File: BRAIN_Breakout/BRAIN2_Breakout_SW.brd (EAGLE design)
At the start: 96.9 x 68.4 mm, 101 parts

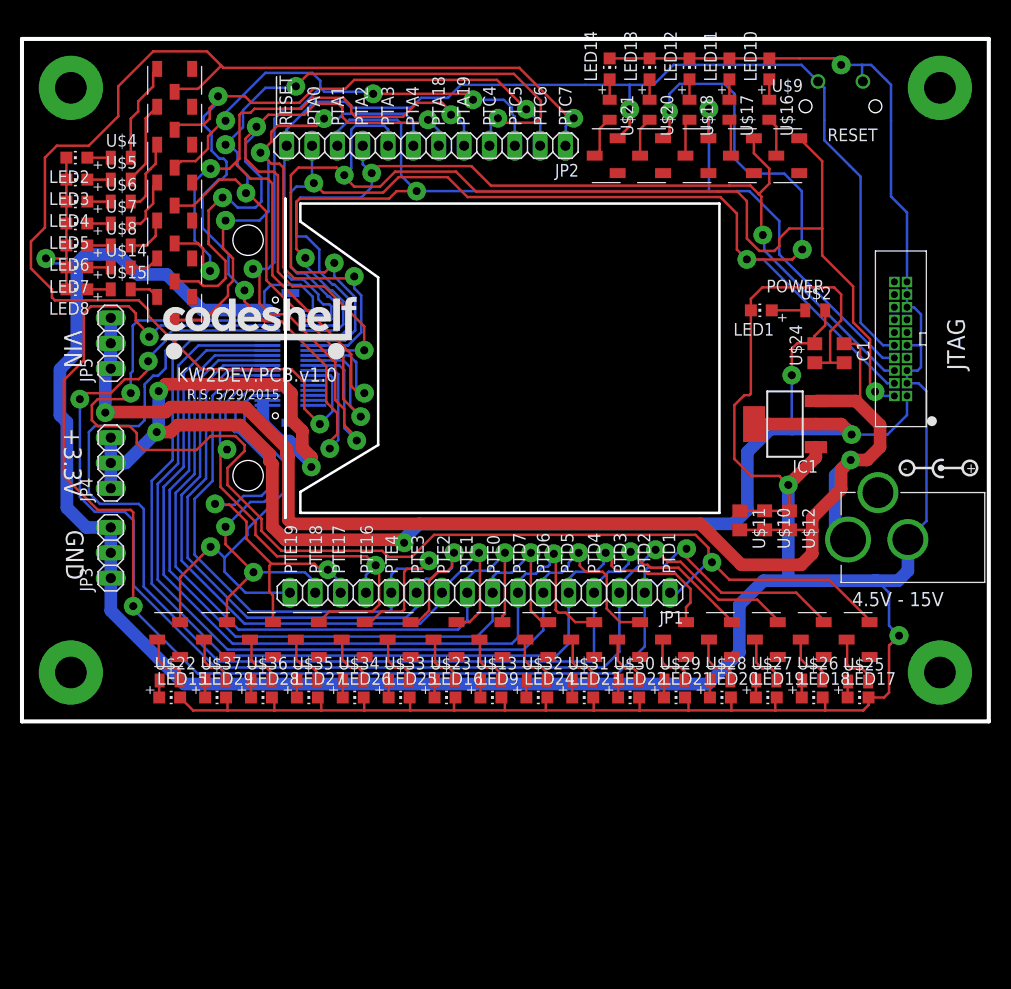
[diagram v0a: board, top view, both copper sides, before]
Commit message: Added board for new KW2
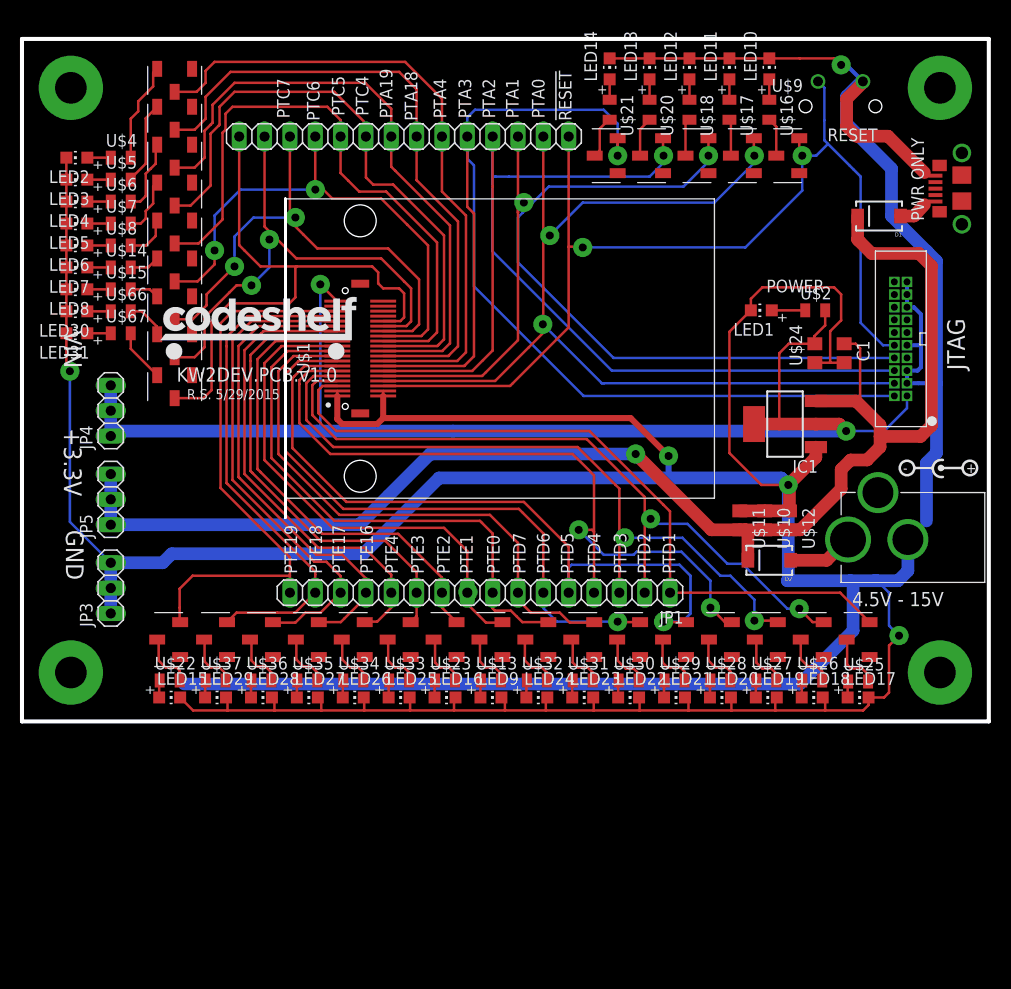
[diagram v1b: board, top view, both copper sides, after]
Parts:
- added D1, D2: (no value), SparkFun:SMA-DIODE
- added LED30, LED31: (no value), adafruit:CHIP-LED0805
- added U$66, U$67: (no value), GW-devices:RF-C0805
- added U$68, U$69: CJS, KW2:CJS
- added X1: USB, SparkFun:USB3076-30-A
- JP2: device pinhead:1X12 -> pinhead:1X14
- U$1: value DF12_F -> KW2_CPU_NEW; device KW2:DF12_F -> KW2:BRAIN_NEW
- U$2: value (none) -> 1k
- U$21: value (none) -> 2k
- moved JP5 15.6 mm to (42.0, 35.4)
- moved U$1 7.06 mm to (67.0, 50.5), flipped to the top, turned to 90 degrees
- moved JP4 5.24 mm to (42.0, 44.2)
- moved JP3 3.54 mm to (42.0, 26.5)
- moved JP2 2.40 mm to (71.4, 71.7), turned to 0 degrees
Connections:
- removed net N$51: JP2.9, U$1.P$12, U$19.P$6, U$55.P$3
- new net N$71: D2.A, U$3.P$1
- new net N$72: D1.A, X1.VCC
- new net N$73: JP2.1, U$1.P$32, U$69.P$1
- new net N$75: LED30.A, U$66.1
- new net N$76: LED31.A, U$67.1
- new net N$77: U$67.2, U$69.P$3
- new net N$78: U$66.2, U$68.P$3
- new net N$80: JP2.2, U$1.P$30, U$68.P$1
- new net N$86: JP2.11, U$1.P$12, U$19.P$6, U$57.P$3
- net GND: now also LED30.C, LED31.C, X1.GND
- net N$21: now also JP2.3, U$65.P$1; no longer JP2.1, U$59.P$1
- net N$22: now also JP2.4, U$64.P$1; no longer JP2.2, U$60.P$1
- net N$23: now also JP2.5, U$63.P$1; no longer JP2.3, U$61.P$1
- net N$24: now also JP2.6; no longer JP2.4
- net N$25: now also JP2.7, U$61.P$1; no longer JP2.5, U$63.P$1
- net N$26: now also JP2.8, U$60.P$1; no longer JP2.6, U$64.P$1
- net N$27: now also JP2.9, U$59.P$1; no longer JP2.7, U$65.P$1
- net N$48: now also JP2.10, U$58.P$3; no longer JP2.8, U$54.P$3
- net N$54: now also JP2.12; no longer JP2.10
- net N$57: now also JP2.13, U$55.P$3; no longer JP2.11, U$57.P$3
- net N$60: now also JP2.14, U$54.P$3; no longer JP2.12, U$58.P$3
- net V+: now also D1.C, D2.C; no longer U$3.P$1
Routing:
- net N$86: track 0.00 -> 110.5 mm, vias 0 -> 1
- net N$51: track 102.9 -> 0.00 mm, vias 2 -> 0
- net GND: track 436.8 -> 533.9 mm, vias 4 -> 5
- net N$21: track 127.5 -> 51.5 mm
- net PTD2: track 141.5 -> 74.2 mm, vias 3 -> 2
- net N$73: track 0.00 -> 58.2 mm
- net PTD1: track 128.0 -> 73.1 mm, vias 2 -> 0
- net PTD3: track 125.1 -> 72.4 mm, vias 3 -> 2
- net N$80: track 0.00 -> 50.9 mm, vias 0 -> 2
- net N$22: track 99.8 -> 53.2 mm, vias 4 -> 2
- net PTD4: track 119.7 -> 74.6 mm, vias 1 -> 2
- net N$23: track 100.8 -> 61.5 mm, vias 5 -> 0
- net +3V3: track 167.8 -> 129.7 mm, vias 6 -> 2
- net N$24: track 98.1 -> 61.7 mm, vias 5 -> 0
- net PTD6: track 96.0 -> 60.5 mm
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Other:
- outline, holes or cut-outs redrawn
- board text added: "PWR ONLY"

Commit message: sync repo
Get the DEVBDS work in sync
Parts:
- added IC2: FT2232HL, KW2:LQFP64
- moved LED1 7.03 mm to (109.0, 47.5), turned to 270 degrees
- moved U$2 6.00 mm to (109.0, 49.5)
- moved C1 1.50 mm to (115.5, 48.5)
- moved U$24 1.50 mm to (112.6, 48.5)
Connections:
- new net N$82: X1.D-
- new net N$83: X1.D+
- net GND: now also X1.P$4
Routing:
- net +3V3: track 129.7 -> 117.4 mm
- net GND: track 533.9 -> 525.9 mm
- net N$1: track 3.35 -> 2.02 mm
- net V+: track 145.3 -> 144.1 mm
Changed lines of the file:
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@@
 <setting verticaltext="up"/>
 </settings>
-<grid distance="1" unitdist="mm" unit="mm" style="lines" multiple="1" display="yes" altdistance="0.05" altunitdist="mm" altunit="mm"/>
+<grid distance="0.5" unitdist="mm" unit="mm" style="lines" multiple="1" display="yes" altdistance="0.05" altunitdist="mm" altunit="mm"/>
 <layers>
 <layer number="1" name="Top" color="4" fill="1" visible="yes" active="yes"/>
@@
 <attribute name="MFGP" value="NCP1117ST33T3G" x="109.57" y="42.9" size="1.778" layer="27" rot="R90" display="off"/>
 </element>
-<element name="U$24" library="GW-devices" package="C0805" value="" x="112.56" y="50" rot="R90">
-<attribute name="MFGN" value="Murata" x="112.56" y="50" size="1.778" layer="27" rot="R90" display="off"/>
-<attribute name="MFGP" value="GRM219R61E106KA12D" x="112.56" y="50" size="1.778" layer="27" rot="R90" display="off"/>
+<element name="U$24" library="GW-devices" package="C0805" value="" x="112.56" y="48.5" rot="R90">
+<attribute name="MFGN" value="Murata" x="112.56" y="48.5" size="1.778" layer="27" rot="R90" display="off"/>
+<attribute name="MFGP" value="GRM219R61E106KA12D" x="112.56" y="48.5" size="1.778" layer="27" rot="R90" display="off"/>
 </element>
 <element name="U$3" library="KW2" package="BARREL_CUI_PJ-002A" value="BARREL_CUI_PJ-002A" x="115.89" y="31.33" smashed="yes">
@@
 <attribute name="MFGP" value="PRPC003SAAN-RC" x="42" y="35.35" size="1.778" layer="27" rot="R90" display="off"/>
 </element>
-<element name="LED1" library="adafruit" package="CHIP-LED0805" value="" x="107.2" y="54.3" rot="R90">
-<attribute name="MFGN" value="Wurth Electronics Inc" x="107.2" y="54.3" size="1.778" layer="27" rot="R90" display="off"/>
-<attribute name="MFGP" value="150080BS75000" x="107.2" y="54.3" size="1.778" layer="27" rot="R90" display="off"/>
-</element>
-<element name="U$2" library="GW-devices" package="RF-C0805" value="1k" x="112.6" y="54.3">
-<attribute name="MFGN" value="Panasonic" x="112.6" y="54.3" size="1.778" layer="27" display="off"/>
-<attribute name="MFGP" value="ERJ-6ENF2000V" x="112.6" y="54.3" size="1.778" layer="27" display="off"/>
+<element name="LED1" library="adafruit" package="CHIP-LED0805" value="" x="109" y="47.5" rot="R270">
+<attribute name="MFGN" value="Wurth Electronics Inc" x="109" y="47.5" size="1.778" layer="27" rot="R270" display="off"/>
+<attribute name="MFGP" value="150080BS75000" x="109" y="47.5" size="1.778" layer="27" rot="R270" display="off"/>
+</element>
+<element name="U$2" library="GW-devices" package="RF-C0805" value="1k" x="109" y="49.5">
+<attribute name="MFGN" value="Panasonic" x="109" y="49.5" size="1.778" layer="27" display="off"/>
+<attribute name="MFGP" value="ERJ-6ENF2000V" x="109" y="49.5" size="1.778" layer="27" display="off"/>
 </element>
 <element name="LED2" library="adafruit" package="CHIP-LED0805" value="" x="38.6" y="69.6" rot="R90">
@@
 <attribute name="MFGP" value="ERJ-6ENF2001V" x="43" y="56.4" size="1.778" layer="27" display="off"/>
 </element>
-<element name="C1" library="GW-devices" package="C0805" value="" x="115.5" y="50" rot="R270">
-<attribute name="MFGN" value="Murata" x="115.5" y="50" size="1.778" layer="27" rot="R270" display="off"/>
-<attribute name="MFGP" value="GRM219R61E106KA12D" x="115.5" y="50" size="1.778" layer="27" rot="R270" display="off"/>
+<element name="C1" library="GW-devices" package="C0805" value="" x="115.5" y="48.5" rot="R270">
+<attribute name="MFGN" value="Murata" x="115.5" y="48.5" size="1.778" layer="27" rot="R270" display="off"/>
+<attribute name="MFGP" value="GRM219R61E106KA12D" x="115.5" y="48.5" size="1.778" layer="27" rot="R270" display="off"/>
 </element>
 <element name="LED9" library="adafruit" package="CHIP-LED0805" value="" x="80.1" y="15.5" rot="R270">
@@
 <attribute name="MFGP" value="CJS-1200TA" x="66.4" y="50.9" size="1.778" layer="27" rot="R180" display="off"/>
 </element>
+<element name="IC2" library="KW2" package="LQFP64" value="FT2232HL" x="73.5" y="-5.5"/>
 </elements>
 <signals>
@@
 <wire x1="121.89" y1="31.33" x2="121.89" y2="28.19" width="1.27" layer="16"/>
 <wire x1="121.89" y1="28.19" x2="120.9" y2="27.2" width="1.27" layer="16"/>
-<wire x1="112.56" y1="49.05" x2="114.1" y2="49.05" width="0.254" layer="1"/>
-<wire x1="114.1" y1="49.05" x2="115.5" y2="49.05" width="0.254" layer="1"/>
+<wire x1="112.56" y1="47.55" x2="114" y2="47.55" width="0.254" layer="1"/>
+<wire x1="114" y1="47.55" x2="114.1" y2="47.55" width="0.254" layer="1"/>
+<wire x1="114.1" y1="47.55" x2="115.5" y2="47.55" width="0.254" layer="1"/>
 <wire x1="120.9" y1="27.2" x2="118.8" y2="27.2" width="1.27" layer="16"/>
 <wire x1="118.8" y1="27.2" x2="118.5" y2="27.2" width="1.27" layer="16"/>
@@
 <contactref element="LED28" pad="C"/>
 <contactref element="LED29" pad="C"/>
-<wire x1="106.15" y1="54.3" x2="106.15" y2="55.45" width="0.254" layer="1"/>
-<wire x1="106.15" y1="55.45" x2="107.3" y2="56.6" width="0.254" layer="1"/>
-<wire x1="107.3" y1="56.6" x2="114.5" y2="56.6" width="0.254" layer="1"/>
-<wire x1="114.1" y1="52.2" x2="114.1" y2="49.05" width="0.254" layer="1"/>
 <wire x1="123.75" y1="33.19" x2="121.89" y2="31.33" width="0.4064" layer="16"/>
 <wire x1="48.95" y1="15.5" x2="50.25" y2="14.2" width="0.254" layer="1"/>
@@
 <wire x1="121.8" y1="55.88" x2="121.8" y2="54.61" width="0.4064" layer="16"/>
 <wire x1="123.1" y1="50.8" x2="123.2" y2="50.7" width="0.4064" layer="16"/>
-<wire x1="114.5" y1="56.6" x2="115.2" y2="55.9" width="0.254" layer="1"/>
-<wire x1="115.2" y1="55.9" x2="115.2" y2="53.3" width="0.254" layer="1"/>
-<wire x1="115.2" y1="53.3" x2="114.1" y2="52.2" width="0.254" layer="1"/>
 <wire x1="118.8" y1="27.2" x2="120" y2="26" width="0.254" layer="16"/>
 <wire x1="111.05" y1="79.55" x2="114.55" y2="79.55" width="0.254" layer="1"/>
@@
 <wire x1="97.9" y1="39.7" x2="97.9" y2="37.6" width="0.6096" layer="16"/>
 <wire x1="97.9" y1="37.6" x2="98" y2="37.5" width="0.254" layer="16"/>
-<wire x1="106.15" y1="54.3" x2="104" y2="52.15" width="0.254" layer="1"/>
-<wire x1="104" y1="52.15" x2="104" y2="40" width="0.254" layer="1"/>
-<wire x1="104" y1="40" x2="107.2" y2="36.8" width="0.254" layer="1"/>
-<wire x1="107.2" y1="36.8" x2="109.9" y2="36.8" width="0.254" layer="1"/>
 <wire x1="37.55" y1="60.8" x2="37.55" y2="58.6" width="0.254" layer="1"/>
+<contactref element="X1" pad="P$4"/>
+<wire x1="124.65" y1="67.8" x2="124.65" y2="67.15" width="0.4064" layer="1"/>
+<wire x1="110.05" y1="47.5" x2="112.51" y2="47.5" width="0.254" layer="1"/>
+<wire x1="112.51" y1="47.5" x2="112.56" y2="47.55" width="0.254" layer="1"/>
+<wire x1="109.9" y1="36.8" x2="107.2" y2="36.8" width="0.254" layer="1"/>
+<wire x1="107.2" y1="36.8" x2="104.5" y2="39.5" width="0.254" layer="1"/>
+<wire x1="104.5" y1="39.5" x2="104.5" y2="45" width="0.254" layer="1"/>
+<wire x1="104.5" y1="45" x2="105.5" y2="46" width="0.254" layer="1"/>
+<wire x1="105.5" y1="46" x2="106" y2="46" width="0.254" layer="1"/>
+<wire x1="106" y1="46" x2="106.5" y2="46.5" width="0.254" layer="1"/>
+<wire x1="106.5" y1="46.5" x2="106.5" y2="50.5" width="0.254" layer="1"/>
+<wire x1="106.5" y1="50.5" x2="107" y2="51" width="0.254" layer="1"/>
+<wire x1="107" y1="51" x2="113.5" y2="51" width="0.254" layer="1"/>
+<wire x1="113.5" y1="51" x2="114" y2="50.5" width="0.254" layer="1"/>
+<wire x1="114" y1="50.5" x2="114" y2="47.55" width="0.254" layer="1"/>
 </signal>
 <signal name="+3V3">
@@
 <wire x1="64.7" y1="55.22" x2="64.7" y2="54.72" width="0.254" layer="1"/>
 <contactref element="U$2" pad="2"/>
-<wire x1="113.6" y1="54.3" x2="113.6" y2="52.8" width="0.254" layer="1"/>
-<wire x1="113.6" y1="52.8" x2="112.5" y2="51.7" width="0.254" layer="1"/>
-<wire x1="112.5" y1="51.7" x2="112.5" y2="51.01" width="0.254" layer="1"/>
-<wire x1="112.5" y1="51.01" x2="112.56" y2="50.95" width="0.254" layer="1"/>
+<wire x1="112.5" y1="49.51" x2="112.56" y2="49.45" width="0.254" layer="1"/>
 <wire x1="106.471" y1="42.9" x2="109" y2="42.9" width="1.27" layer="1"/>
 <wire x1="109" y1="42.9" x2="112.6688" y2="42.9" width="1.27" layer="1"/>
@@
 <wire x1="119.7" y1="42.4" x2="119.5" y2="42.2" width="0.254" layer="16"/>
 <wire x1="119.5" y1="42.2" x2="115.7" y2="42.2" width="0.254" layer="16"/>
-<wire x1="112.56" y1="50.95" x2="109.95" y2="50.95" width="0.254" layer="1"/>
-<wire x1="109.95" y1="50.95" x2="109" y2="50" width="0.254" layer="1"/>
-<wire x1="109" y1="50" x2="109" y2="42.9" width="0.254" layer="1"/>
+<wire x1="112.56" y1="49.45" x2="110.05" y2="49.45" width="0.254" layer="1"/>
+<wire x1="110.05" y1="49.45" x2="110" y2="49.5" width="0.254" layer="1"/>
+<wire x1="112.6688" y1="42.9" x2="112.56" y2="49.45" width="0" layer="19" extent="1-1"/>
 </signal>
 <signal name="V+">
@@
 <wire x1="115.2" y1="38.35" x2="116.15" y2="39.3" width="1.27" layer="1"/>
 <wire x1="112.6688" y1="45.2114" x2="116.6886" y2="45.2114" width="1.27" layer="1"/>
-<wire x1="115.5" y1="50.95" x2="116.65" y2="50.95" width="0.254" layer="1"/>
-<wire x1="116.65" y1="50.95" x2="117.1" y2="50.5" width="0.254" layer="1"/>
-<wire x1="117.1" y1="50.5" x2="117.1" y2="45.6228" width="0.254" layer="1"/>
+<wire x1="115.5" y1="49.45" x2="116.65" y2="49.45" width="0.254" layer="1"/>
+<wire x1="116.65" y1="49.45" x2="117.1" y2="49.5" width="0.254" layer="1"/>
+<wire x1="117.1" y1="49.5" x2="117.1" y2="45.6228" width="0.254" layer="1"/>
 <wire x1="117.1" y1="45.6228" x2="116.6886" y2="45.2114" width="0.254" layer="1"/>
 <wire x1="111.1" y1="32.3" x2="112.3" y2="33.5" width="1.27" layer="1"/>
@@
 <contactref element="LED1" pad="A"/>
 <contactref element="U$2" pad="1"/>
-<wire x1="108.25" y1="54.3" x2="111.6" y2="54.3" width="0.254" layer="1"/>
+<wire x1="108" y1="49.5" x2="108" y2="47.55" width="0.254" layer="1"/>
+<wire x1="108" y1="47.55" x2="107.95" y2="47.5" width="0.254" layer="1"/>
 </signal>
 <signal name="N$2">
@@
 <signal name="N$51">
 </signal>
+<signal name="N$82">
+<contactref element="X1" pad="D-"/>
+</signal>
+<signal name="N$83">
+<contactref element="X1" pad="D+"/>
+</signal>
 </signals>
